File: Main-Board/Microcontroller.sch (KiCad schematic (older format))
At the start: 34 parts, among them J8 USB_B_Micro, J9 ICSP, SW1 Reset, U3 FT232RL, U4 ATmega328P-AU, U5 LM1117-5.0, Y1 16 MHz

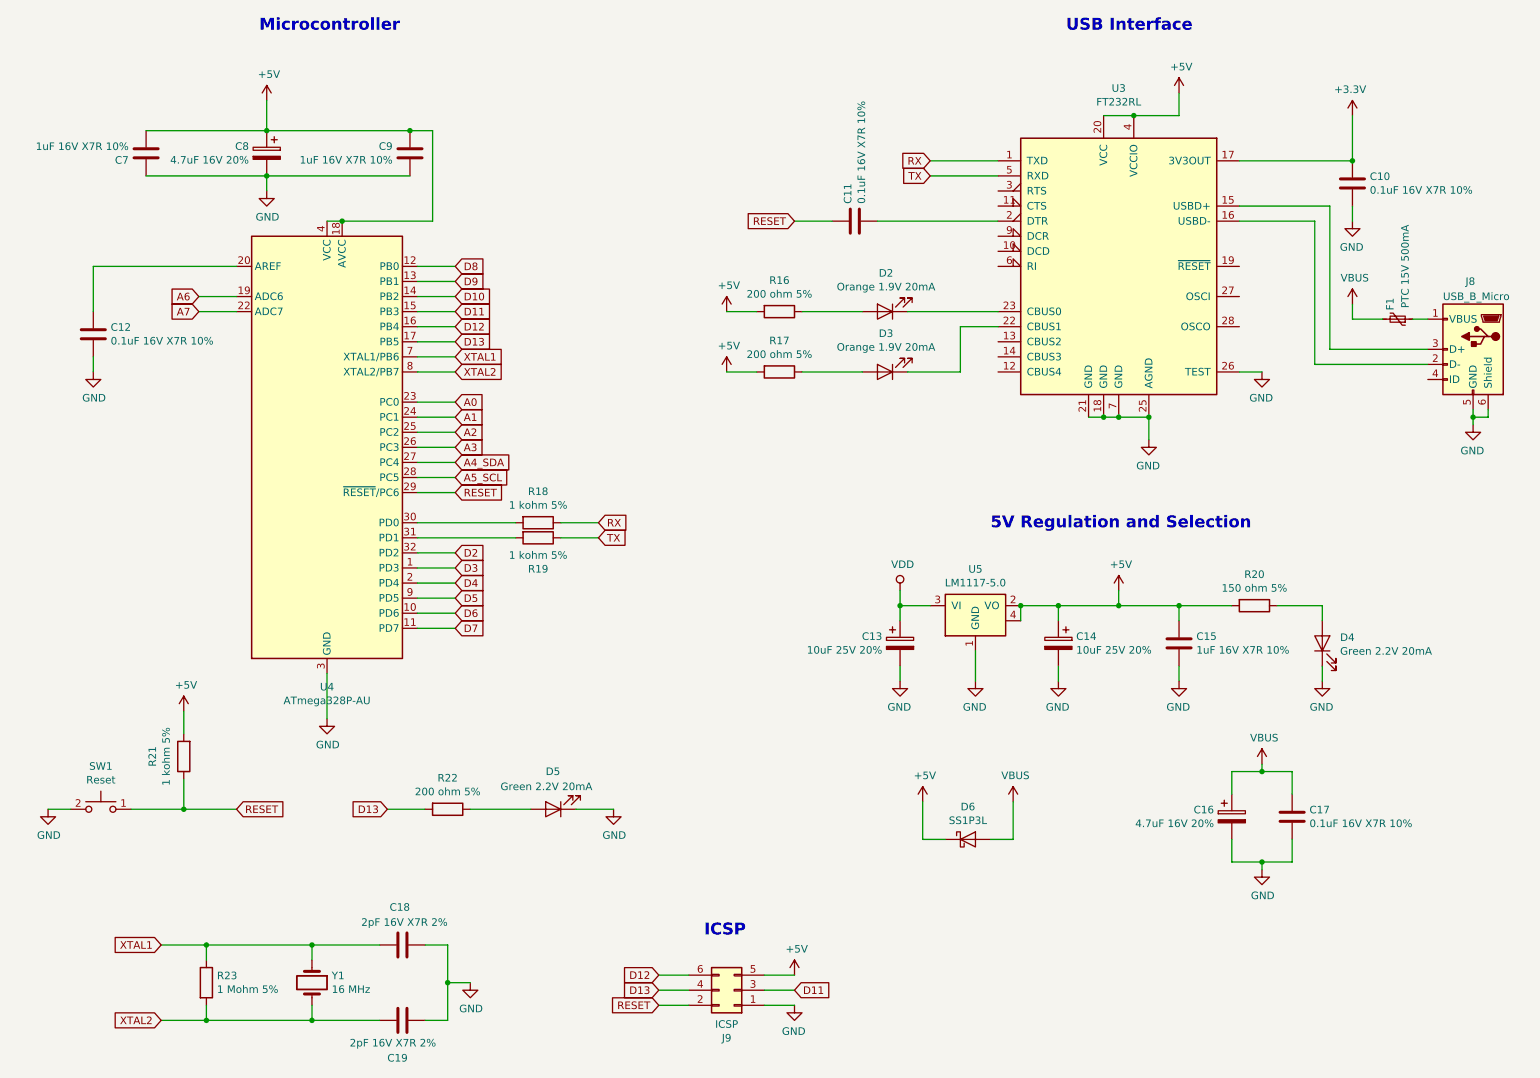
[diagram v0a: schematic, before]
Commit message: Switched from crystal to Resonator
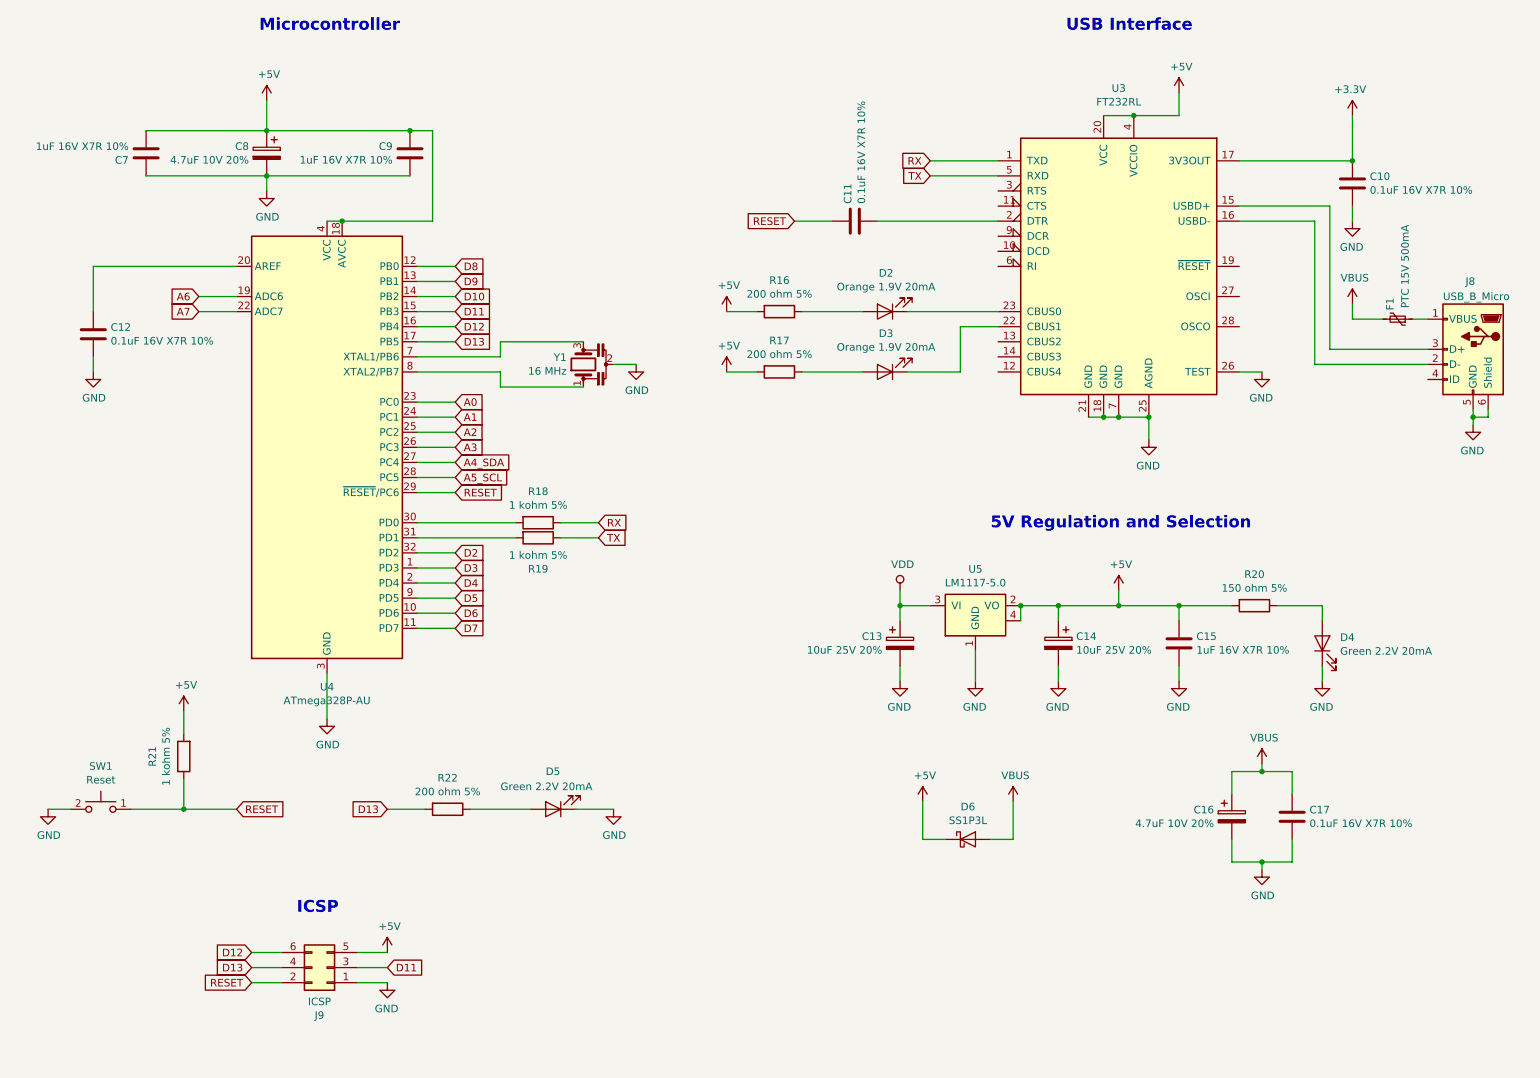
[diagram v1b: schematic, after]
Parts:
- removed C18, C19: 2pF 16V X7R 2%, Capacitor_SMD:C_0603_1608Metric_Pad1.05x0.95mm_HandSolder, symbol Device:C
- removed R23: 1 Mohm 5%, Resistor_SMD:R_0603_1608Metric_Pad1.05x0.95mm_HandSolder, symbol Device:R
- removed Y1: 16 MHz, Custom:Crystal, symbol Device:Crystal
- added Y1: 16 MHz, Custom:Resonator, symbol Device:Resonator
- C16, C8: value 4.7uF 16V 20% -> 4.7uF 10V 20%
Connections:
- net GND: now also Y1.2
- net XTAL1: no longer names the net of U4.7 (XTAL1/PB6)
- net XTAL1: now also Y1.3
- net XTAL2: no longer names the net of U4.8 (XTAL2/PB7)
- net XTAL2: now also Y1.1
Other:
- moved on the sheet: J9
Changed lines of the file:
@@
 L Connector_Generic:Conn_02x03_Odd_Even J9
 U 1 1 5FE91946
-P 5300 7100
-F 0 "J9" H 5350 7417 50  0000 C CNN
-F 1 "ICSP" H 5350 7326 50  0000 C CNN
-F 2 "Connector_PinHeader_2.54mm:PinHeader_2x03_P2.54mm_Vertical" H 5300 7100 50  0001 C CNN
-F 3 "~" H 5300 7100 50  0001 C CNN
-	1    5300 7100
+P 2600 6950
+F 0 "J9" H 2650 7267 50  0000 C CNN
+F 1 "ICSP" H 2650 7176 50  0000 C CNN
+F 2 "Connector_PinHeader_2.54mm:PinHeader_2x03_P2.54mm_Vertical" H 2600 6950 50  0001 C CNN
+F 3 "~" H 2600 6950 50  0001 C CNN
+	1    2600 6950
 	-1   0    0    1
 $EndComp
-Text GLabel 4800 7200 0    50   Input ~ 0
+Text GLabel 2100 7050 0    50   Input ~ 0
 RESET
 $Comp
 L power:GND #PWR066
 U 1 1 5FE94089
-P 5700 7200
-F 0 "#PWR066" H 5700 6950 50  0001 C CNN
-F 1 "GND" H 5705 7027 50  0000 C CNN
-F 2 "" H 5700 7200 50  0001 C CNN
-F 3 "" H 5700 7200 50  0001 C CNN
-	1    5700 7200
+P 3000 7050
+F 0 "#PWR066" H 3000 6800 50  0001 C CNN
+F 1 "GND" H 3005 6877 50  0000 C CNN
+F 2 "" H 3000 7050 50  0001 C CNN
+F 3 "" H 3000 7050 50  0001 C CNN
+	1    3000 7050
 	-1   0    0    -1
 $EndComp
 Wire Wire Line
-	4800 7200 5000 7200
-Wire Wire Line
-	5500 7200 5700 7200
+	2100 7050 2300 7050
+Wire Wire Line
+	2800 7050 3000 7050
 $Comp
 L power:+5V #PWR064
 U 1 1 5FE9C160
-P 5700 7000
-F 0 "#PWR064" H 5700 6850 50  0001 C CNN
-F 1 "+5V" H 5715 7173 50  0000 C CNN
-F 2 "" H 5700 7000 50  0001 C CNN
-F 3 "" H 5700 7000 50  0001 C CNN
-	1    5700 7000
-	1    0    0    -1
-$EndComp
-Text GLabel 5700 7100 2    50   Input ~ 0
+P 3000 6850
+F 0 "#PWR064" H 3000 6700 50  0001 C CNN
+F 1 "+5V" H 3015 7023 50  0000 C CNN
+F 2 "" H 3000 6850 50  0001 C CNN
+F 3 "" H 3000 6850 50  0001 C CNN
+	1    3000 6850
+	1    0    0    -1
+$EndComp
+Text GLabel 3000 6950 2    50   Input ~ 0
 D11
-Text GLabel 4800 7000 0    50   Input ~ 0
+Text GLabel 2100 6850 0    50   Input ~ 0
 D12
-Text GLabel 4800 7100 0    50   Input ~ 0
+Text GLabel 2100 6950 0    50   Input ~ 0
 D13
 Wire Wire Line
-	4800 7000 5000 7000
-Wire Wire Line
-	5000 7100 4800 7100
-Wire Wire Line
-	5500 7000 5700 7000
-Wire Wire Line
-	5700 7100 5500 7100
+	2100 6850 2300 6850
+Wire Wire Line
+	2300 6950 2100 6950
+Wire Wire Line
+	2800 6850 3000 6850
+Wire Wire Line
+	3000 6950 2800 6950
 $Comp
 L power:GND #PWR061
@@
 P 2200 1550
 F 0 "C8" H 2318 1596 50  0000 L CNN
-F 1 "4.7uF 16V 20%" H 2318 1505 50  0000 L CNN
+F 1 "4.7uF 10V 20%" H 2318 1505 50  0000 L CNN
 F 2 "Capacitor_SMD:C_0603_1608Metric_Pad1.05x0.95mm_HandSolder" H 2238 1400 50  0001 C CNN
 F 3 "~" H 2200 1550 50  0001 C CNN
@@
 P 8600 5950
 F 0 "C16" H 8482 5996 50  0000 R CNN
-F 1 "4.7uF 16V 20%" H 8482 5905 50  0000 R CNN
+F 1 "4.7uF 10V 20%" H 8482 5905 50  0000 R CNN
 F 2 "Capacitor_SMD:C_0603_1608Metric_Pad1.05x0.95mm_HandSolder" H 8638 5800 50  0001 C CNN
 F 3 "~" H 8600 5950 50  0001 C CNN
@@
 Wire Wire Line
 	3550 5900 3950 5900
-Text Notes 5100 6750 0    79   ~ 16
+Text Notes 2400 6600 0    79   ~ 16
 ICSP
-Text GLabel 3450 2900 2    50   Input ~ 0
-XTAL1
-Text GLabel 3450 3000 2    50   Input ~ 0
-XTAL2
-Wire Wire Line
-	3450 2900 3200 2900
-Wire Wire Line
-	3200 3000 3450 3000
-$Comp
-L power:GND #PWR065
-U 1 1 5FEC1FF5
-P 3550 7050
-F 0 "#PWR065" H 3550 6800 50  0001 C CNN
-F 1 "GND" H 3555 6877 50  0000 C CNN
-F 2 "" H 3550 7050 50  0001 C CNN
-F 3 "" H 3550 7050 50  0001 C CNN
-	1    3550 7050
-	1    0    0    -1
-$EndComp
-$Comp
-L Device:Crystal Y1
-U 1 1 6031835C
-P 2500 7050
-F 0 "Y1" V 2454 7181 50  0000 L CNN
-F 1 "16 MHz" V 2545 7181 50  0000 L CNN
-F 2 "Custom:Crystal" H 2500 7050 50  0001 C CNN
-F 3 "~" H 2500 7050 50  0001 C CNN
-F 4 "Fox Electronics" H 2500 7050 50  0001 C CNN "Manufacturer"
-F 5 "FC4STCBMF16.0-BAG200" H 2500 7050 50  0001 C CNN "Manufacturer #"
-F 6 "631-1108-ND" H 2500 7050 50  0001 C CNN "Digi-Key #"
-F 7 "https://www.digikey.ca/en/products/detail/fox-electronics/FC4STCBMF16-0-BAG200/1024700?s=N4IgTCBcDaIGIHkAaBlAMnA9ARgGwAYBaMfEAXQF8g" H 2500 7050 50  0001 C CNN "Digi-Key LinkDigi LinkDigi-Key Link"
-	1    2500 7050
-	0    1    1    0
-$EndComp
-$Comp
-L Device:R R23
-U 1 1 60339A37
-P 1800 7050
-F 0 "R23" H 1870 7096 50  0000 L CNN
-F 1 "1 Mohm 5%" H 1870 7005 50  0000 L CNN
-F 2 "Resistor_SMD:R_0603_1608Metric_Pad1.05x0.95mm_HandSolder" V 1730 7050 50  0001 C CNN
-F 3 "~" H 1800 7050 50  0001 C CNN
-	1    1800 7050
-	1    0    0    -1
-$EndComp
-$Comp
-L Device:C C?
-U 1 1 603531AF
-P 3100 6800
-AR Path="/5FD99B6C/603531AF" Ref="C?"  Part="1"
-AR Path="/5FD9E07D/603531AF" Ref="C?"  Part="1"
-AR Path="/5FDD4B9C/603531AF" Ref="C18"  Part="1"
-F 0 "C18" V 3350 6750 50  0000 L CNN
-F 1 "2pF 16V X7R 2%" V 3250 6500 50  0000 L CNN
-F 2 "Capacitor_SMD:C_0603_1608Metric_Pad1.05x0.95mm_HandSolder" H 3138 6650 50  0001 C CNN
-F 3 "~" H 3100 6800 50  0001 C CNN
-	1    3100 6800
-	0    -1   -1   0
-$EndComp
-$Comp
-L Device:C C?
-U 1 1 60362846
-P 3100 7300
-AR Path="/5FD99B6C/60362846" Ref="C?"  Part="1"
-AR Path="/5FD9E07D/60362846" Ref="C?"  Part="1"
-AR Path="/5FDD4B9C/60362846" Ref="C19"  Part="1"
-F 0 "C19" V 3350 7200 50  0000 L CNN
-F 1 "2pF 16V X7R 2%" V 3250 6950 50  0000 L CNN
-F 2 "Capacitor_SMD:C_0603_1608Metric_Pad1.05x0.95mm_HandSolder" H 3138 7150 50  0001 C CNN
-F 3 "~" H 3100 7300 50  0001 C CNN
-	1    3100 7300
-	0    1    1    0
-$EndComp
-Wire Wire Line
-	1800 6900 1800 6800
-Wire Wire Line
-	1800 7300 1800 7200
-Wire Wire Line
-	2500 7200 2500 7300
-Wire Wire Line
-	2500 6900 2500 6800
-Wire Wire Line
-	3250 7300 3400 7300
-Wire Wire Line
-	3250 6800 3400 6800
-Wire Wire Line
-	3400 6800 3400 7050
-Wire Wire Line
-	3550 7050 3400 7050
-Connection ~ 3400 7050
-Wire Wire Line
-	3400 7050 3400 7300
-Wire Wire Line
-	2950 7300 2500 7300
-Connection ~ 2500 7300
-Wire Wire Line
-	2950 6800 2500 6800
-Connection ~ 2500 6800
-Text GLabel 1500 6800 0    50   Input ~ 0
-XTAL1
-Text GLabel 1500 7300 0    50   Input ~ 0
-XTAL2
 $Comp
 L Custom:Push-Switch SW1
@@
 Wire Wire Line
 	7850 4550 8250 4550
-Connection ~ 1800 6800
-Connection ~ 1800 7300
-Wire Wire Line
-	1800 6800 2500 6800
-Wire Wire Line
-	1800 7300 2500 7300
-Wire Wire Line
-	1500 6800 1800 6800
-Wire Wire Line
-	1500 7300 1800 7300
 Wire Wire Line
 	1050 2300 2000 2300
+$Comp
+L Device:Resonator Y1
+U 1 1 60255C7D
+P 4300 2950
+F 0 "Y1" V 4346 3061 50  0000 L CNN
+F 1 "16 MHz" V 4255 3061 50  0000 L CNN
+F 2 "Custom:Resonator" H 4275 2950 50  0001 C CNN
+F 3 "~" H 4275 2950 50  0001 C CNN
+F 4 "Murata Electronics" H 4300 2950 50  0001 C CNN "Manufacturer"
+F 5 "CSTNE16M0VH3L000R0" H 4300 2950 50  0001 C CNN "Manufacturer #"
+F 6 "490-17952-1-ND" H 4300 2950 50  0001 C CNN "Digi-Key #"
+F 7 "https://www.digikey.ca/en/products/detail/murata-electronics/CSTNE16M0VH3L000R0/8747733" H 4300 2950 50  0001 C CNN "Digi-Key LinkDigi LinkDigi-Key Link"
+	1    4300 2950
+	0    -1   -1   0
+$EndComp
+Wire Wire Line
+	3750 2900 3750 2800
+Wire Wire Line
+	3200 2900 3750 2900
+Wire Wire Line
+	3750 3100 4300 3100
+Wire Wire Line
+	3750 2800 4300 2800
+Wire Wire Line
+	3750 3100 3750 3000
+Wire Wire Line
+	3200 3000 3750 3000
+$Comp
+L power:GND #PWR0101
+U 1 1 60296342
+P 4650 2950
+F 0 "#PWR0101" H 4650 2700 50  0001 C CNN
+F 1 "GND" H 4655 2777 50  0000 C CNN
+F 2 "" H 4650 2950 50  0001 C CNN
+F 3 "" H 4650 2950 50  0001 C CNN
+	1    4650 2950
+	1    0    0    -1
+$EndComp
+Wire Wire Line
+	4500 2950 4650 2950
 $EndSCHEMATC

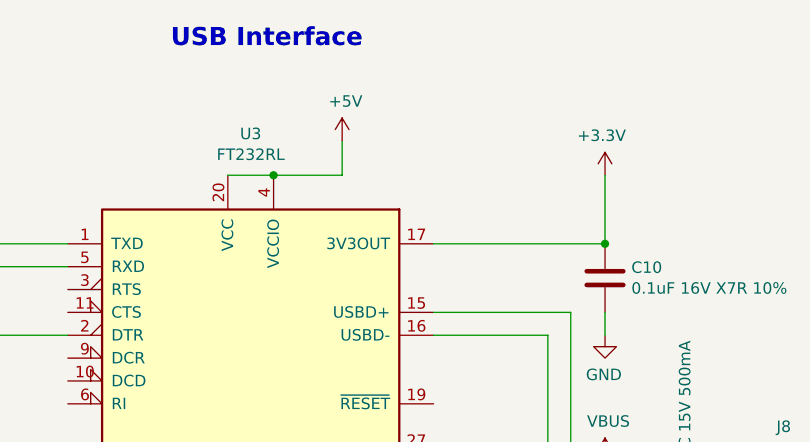
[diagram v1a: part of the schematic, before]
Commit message: add attacheted lights to open ATMEGA ports (A4 cant be used again, dont mess with tx/rx) and removed 5th rc input. Add cap for USB
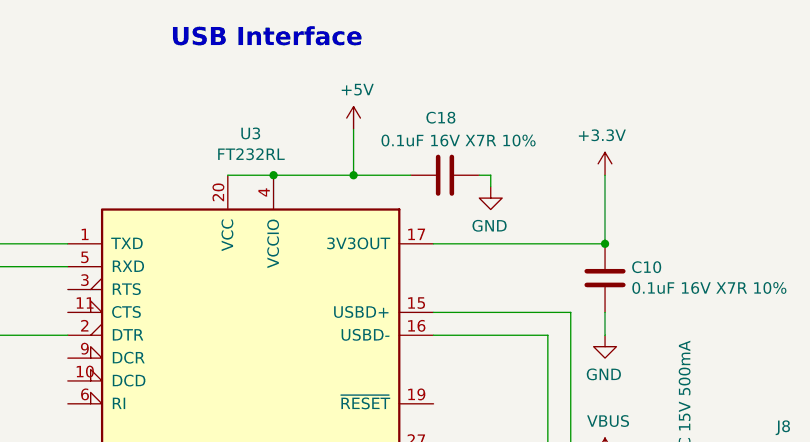
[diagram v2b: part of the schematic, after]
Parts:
- added C18: 0.1uF 16V X7R 10%, Capacitor_SMD:C_0603_1608Metric_Pad1.05x0.95mm_HandSolder, symbol Device:C
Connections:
- net +5V: now also C18.1
- net GND: now also C18.2
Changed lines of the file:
@@
 L power:+5V #PWR037
 U 1 1 5FDF97EF
-P 8250 1150
-F 0 "#PWR037" H 8250 1000 50  0001 C CNN
-F 1 "+5V" H 8265 1323 50  0000 C CNN
-F 2 "" H 8250 1150 50  0001 C CNN
-F 3 "" H 8250 1150 50  0001 C CNN
-	1    8250 1150
+P 8300 1100
+F 0 "#PWR037" H 8300 950 50  0001 C CNN
+F 1 "+5V" H 8315 1273 50  0000 C CNN
+F 2 "" H 8300 1100 50  0001 C CNN
+F 3 "" H 8300 1100 50  0001 C CNN
+	1    8300 1100
 	1    0    0    -1
 $EndComp
 Wire Wire Line
 	7750 1300 7950 1300
-Wire Wire Line
-	7950 1300 8250 1300
-Wire Wire Line
-	8250 1300 8250 1150
 Connection ~ 7950 1300
 Wire Wire Line
@@
 Wire Wire Line
 	4500 2950 4650 2950
+$Comp
+L Device:C C?
+U 1 1 60464E5D
+P 8700 1300
+AR Path="/5FD99B6C/60464E5D" Ref="C?"  Part="1"
+AR Path="/5FD9E07D/60464E5D" Ref="C?"  Part="1"
+AR Path="/5FDD4B9C/60464E5D" Ref="C18"  Part="1"
+F 0 "C18" V 8950 1250 50  0000 L CNN
+F 1 "0.1uF 16V X7R 10%" V 8850 900 50  0000 L CNN
+F 2 "Capacitor_SMD:C_0603_1608Metric_Pad1.05x0.95mm_HandSolder" H 8738 1150 50  0001 C CNN
+F 3 "~" H 8700 1300 50  0001 C CNN
+	1    8700 1300
+	0    -1   -1   0
+$EndComp
+$Comp
+L power:GND #PWR0102
+U 1 1 6048B115
+P 8900 1350
+F 0 "#PWR0102" H 8900 1100 50  0001 C CNN
+F 1 "GND" H 8905 1177 50  0000 C CNN
+F 2 "" H 8900 1350 50  0001 C CNN
+F 3 "" H 8900 1350 50  0001 C CNN
+	1    8900 1350
+	-1   0    0    -1
+$EndComp
+Wire Wire Line
+	8850 1300 8900 1300
+Wire Wire Line
+	8900 1300 8900 1350
+Wire Wire Line
+	7950 1300 8300 1300
+Wire Wire Line
+	8300 1100 8300 1300
+Connection ~ 8300 1300
+Wire Wire Line
+	8300 1300 8550 1300
 $EndSCHEMATC
